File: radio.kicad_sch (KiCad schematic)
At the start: 16 parts, among them J6 Conn_Coaxial, J7 Conn_Coaxial, J8 Conn_Coaxial, U8 SX1262TR8-GC

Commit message: schem: rf fix switchable connectors orientation
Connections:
- net at J7.1 (In): now also TP2.O; no longer TP2.I
- net at TP4.I: now also C17.2, L4.2; no longer J8.1 (In)
- net at C15.1, L3.2: now also TP2.I; no longer TP2.O
- new net: J8.1 (In), TP4.O
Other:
- moved on the sheet: TP2, TP4
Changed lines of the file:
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@@
 	)
 	(junction
-		(at 106.68 73.66)
-		(diameter 0)
-		(color 0 0 0 0)
-	)
-	(junction
 		(at 215.9 104.14)
 		(diameter 0)
@@
 		(color 0 0 0 0)
 	)
+	(junction
+		(at 106.68 73.66)
+		(diameter 0)
+		(color 0 0 0 0)
+	)
 	(wire
 		(pts
@@
 	(wire
 		(pts
-			(xy 111.76 107.95) (xy 111.76 106.68)
+			(xy 121.92 107.95) (xy 121.92 106.68)
 		)
 		(stroke
@@
 	(wire
 		(pts
-			(xy 111.76 106.68) (xy 113.03 106.68)
+			(xy 121.92 106.68) (xy 120.65 106.68)
 		)
 		(stroke
@@
 	(wire
 		(pts
-			(xy 111.76 76.2) (xy 113.03 76.2)
+			(xy 121.92 76.2) (xy 120.65 76.2)
 		)
 		(stroke
@@
 	(wire
 		(pts
-			(xy 123.19 73.66) (xy 124.46 73.66)
+			(xy 120.65 73.66) (xy 124.46 73.66)
 		)
 		(stroke
@@
 	(wire
 		(pts
-			(xy 111.76 77.47) (xy 111.76 76.2)
+			(xy 121.92 77.47) (xy 121.92 76.2)
 		)
 		(stroke
@@
 	(wire
 		(pts
-			(xy 106.68 73.66) (xy 113.03 73.66)
+			(xy 106.68 73.66) (xy 110.49 73.66)
 		)
 		(stroke
@@
 	(wire
 		(pts
-			(xy 123.19 104.14) (xy 124.46 104.14)
+			(xy 120.65 104.14) (xy 124.46 104.14)
 		)
 		(stroke
@@
 	(wire
 		(pts
-			(xy 106.68 104.14) (xy 113.03 104.14)
+			(xy 106.68 104.14) (xy 110.49 104.14)
 		)
 		(stroke
@@
 	(symbol
 		(lib_id "GLCS:RF_switch_connector")
-		(at 118.11 105.41 0)
-		(mirror y)
+		(at 115.57 105.41 0)
 		(unit 1)
 		(body_style 1)
@@
 		(dnp no)
 		(property "Reference" "TP4"
-			(at 118.11 100.33 0)
+			(at 115.57 100.33 0)
 			(show_name no)
 			(do_not_autoplace no)
@@
 		)
 		(property "Value" "RF_switch_connector"
-			(at 118.11 100.33 0)
+			(at 115.57 100.33 0)
 			(hide yes)
 			(show_name no)
@@
 		)
 		(property "Footprint" ""
-			(at 118.11 104.14 0)
+			(at 115.57 104.14 0)
 			(hide yes)
 			(show_name no)
@@
 		)
 		(property "Datasheet" ""
-			(at 118.11 104.14 0)
+			(at 115.57 104.14 0)
 			(hide yes)
 			(show_name no)
@@
 		)
 		(property "Description" "Subminiature Coaxial Switch testpoint"
-			(at 118.11 105.41 0)
+			(at 115.57 105.41 0)
 			(hide yes)
 			(show_name no)
@@
 	(symbol
 		(lib_id "power:GND")
-		(at 111.76 77.47 0)
+		(at 121.92 77.47 0)
+		(mirror y)
 		(unit 1)
 		(body_style 1)
@@
 		(dnp no)
 		(property "Reference" "#PWR046"
-			(at 111.76 83.82 0)
+			(at 121.92 83.82 0)
 			(hide yes)
 			(show_name no)
@@
 		)
 		(property "Value" "GND"
-			(at 114.808 80.264 0)
+			(at 118.872 80.264 0)
 			(hide yes)
 			(show_name no)
@@
 		)
 		(property "Footprint" ""
-			(at 111.76 77.47 0)
+			(at 121.92 77.47 0)
 			(hide yes)
 			(show_name no)
@@
 		)
 		(property "Datasheet" ""
-			(at 111.76 77.47 0)
+			(at 121.92 77.47 0)
 			(hide yes)
 			(show_name no)
@@
 		)
 		(property "Description" "Power symbol creates a global label with name \"GND\" , ground"
-			(at 111.76 77.47 0)
+			(at 121.92 77.47 0)
 			(hide yes)
 			(show_name no)
@@
 	(symbol
 		(lib_id "power:GND")
-		(at 111.76 107.95 0)
+		(at 121.92 107.95 0)
+		(mirror y)
 		(unit 1)
 		(body_style 1)
@@
 		(dnp no)
 		(property "Reference" "#PWR061"
-			(at 111.76 114.3 0)
+			(at 121.92 114.3 0)
 			(hide yes)
 			(show_name no)
@@
 		)
 		(property "Value" "GND"
-			(at 114.808 110.744 0)
+			(at 118.872 110.744 0)
 			(hide yes)
 			(show_name no)
@@
 		)
 		(property "Footprint" ""
-			(at 111.76 107.95 0)
+			(at 121.92 107.95 0)
 			(hide yes)
 			(show_name no)
@@
 		)
 		(property "Datasheet" ""
-			(at 111.76 107.95 0)
+			(at 121.92 107.95 0)
 			(hide yes)
 			(show_name no)
@@
 		)
 		(property "Description" "Power symbol creates a global label with name \"GND\" , ground"
-			(at 111.76 107.95 0)
+			(at 121.92 107.95 0)
 			(hide yes)
 			(show_name no)
@@
 	(symbol
 		(lib_id "GLCS:RF_switch_connector")
-		(at 118.11 74.93 0)
-		(mirror y)
+		(at 115.57 74.93 0)
 		(unit 1)
 		(body_style 1)
@@
 		(dnp no)
 		(property "Reference" "TP2"
-			(at 118.11 69.85 0)
+			(at 115.57 69.85 0)
 			(show_name no)
 			(do_not_autoplace no)
@@
 		)
 		(property "Value" "RF_switch_connector"
-			(at 118.11 69.85 0)
+			(at 115.57 69.85 0)
 			(hide yes)
 			(show_name no)
@@
 		)
 		(property "Footprint" ""
-			(at 118.11 73.66 0)
+			(at 115.57 73.66 0)
 			(hide yes)
 			(show_name no)
@@
 		)
 		(property "Datasheet" ""
-			(at 118.11 73.66 0)
+			(at 115.57 73.66 0)
 			(hide yes)
 			(show_name no)
@@
 		)
 		(property "Description" "Subminiature Coaxial Switch testpoint"
-			(at 118.11 74.93 0)
+			(at 115.57 74.93 0)
 			(hide yes)
 			(show_name no)

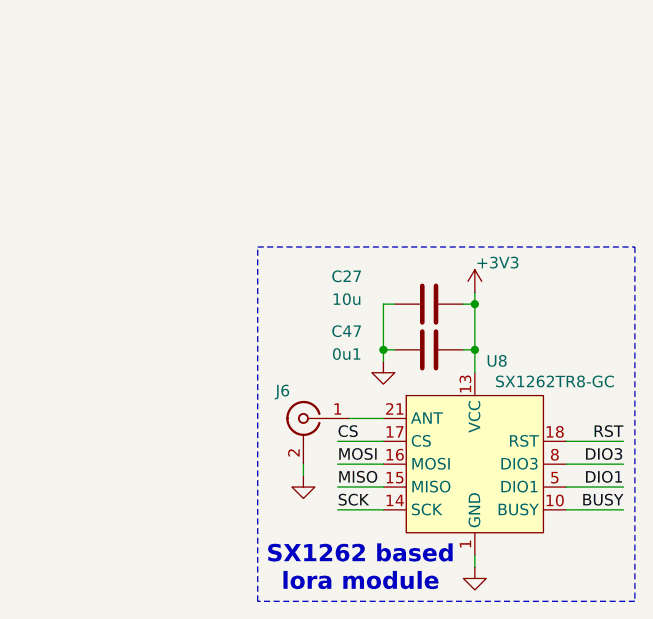
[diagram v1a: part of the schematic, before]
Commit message: schem: add rain/wind schmitt trigger
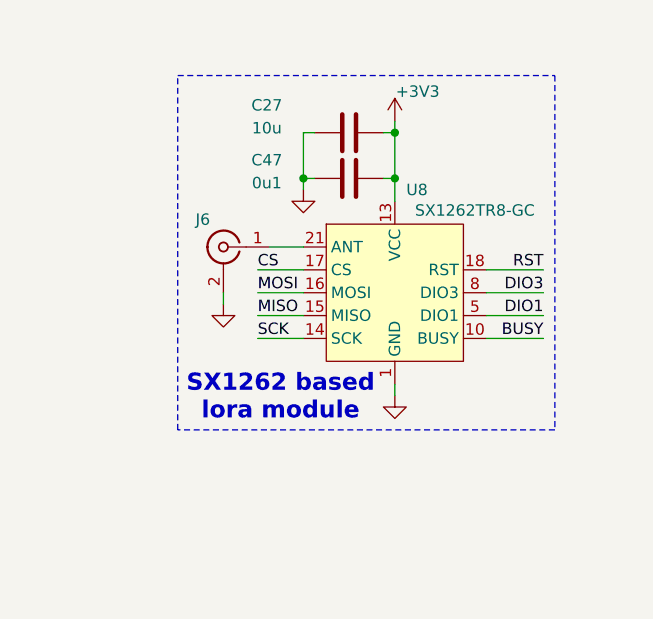
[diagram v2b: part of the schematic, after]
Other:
- moved on the sheet: C27, C47, J6, U8

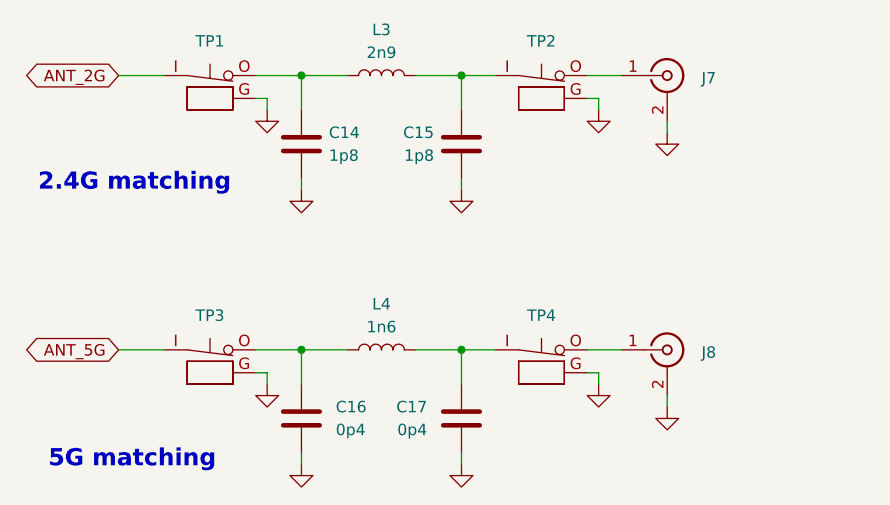
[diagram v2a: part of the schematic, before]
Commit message: schem: remove esp32
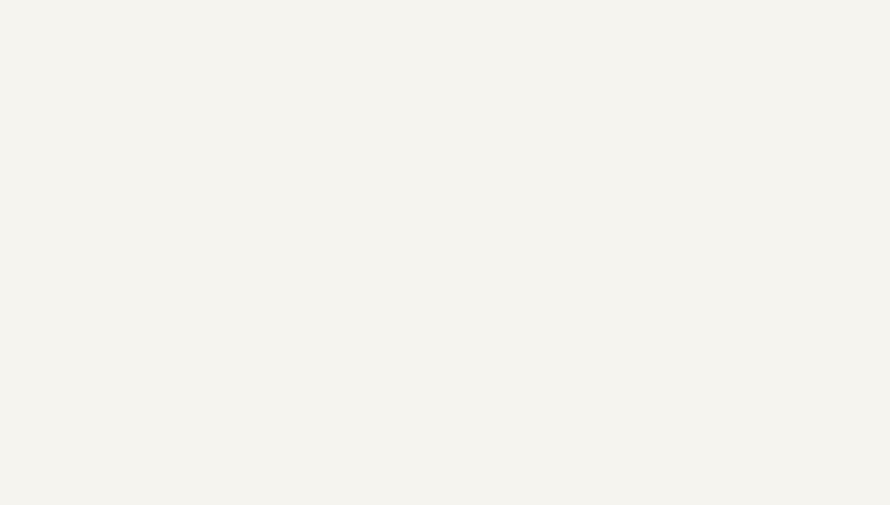
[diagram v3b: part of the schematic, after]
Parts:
- removed C14, C15: 1p8, Capacitor_SMD:C_0402_1005Metric, symbol Device:C
- removed C16, C17: 0p4, symbol Device:C
- removed J7, J8: Conn_Coaxial, symbol Connector:Conn_Coaxial
- removed L3: 2n9, symbol Device:L
- removed L4: 1n6, symbol Device:L
- removed TP1, TP2, TP3, TP4: RF_switch_connector, symbol GLCS:RF_switch_connector
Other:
- note removed: "2.4G matching"
- note removed: "5G matching"
